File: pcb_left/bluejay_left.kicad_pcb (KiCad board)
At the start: 2 copper layers, 148.3 x 140.5 mm, 81 parts, among them J1 SJ-43514, U1 ATmega328P-PU, Y1 16MHz

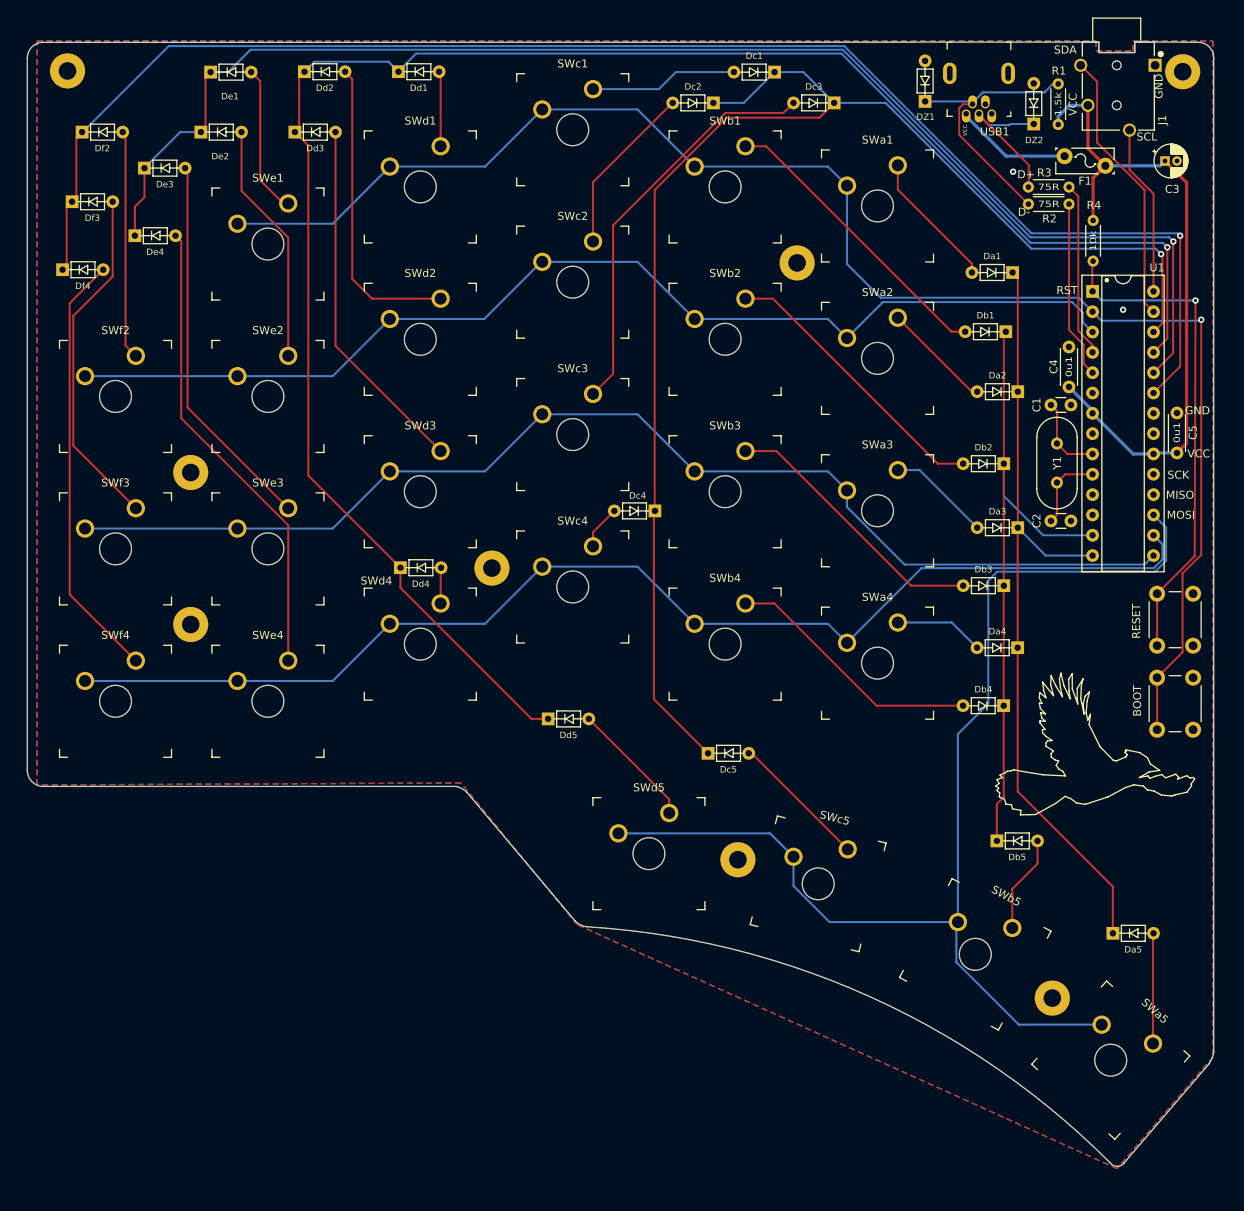
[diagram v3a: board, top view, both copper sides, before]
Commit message: fine tune edge cuts
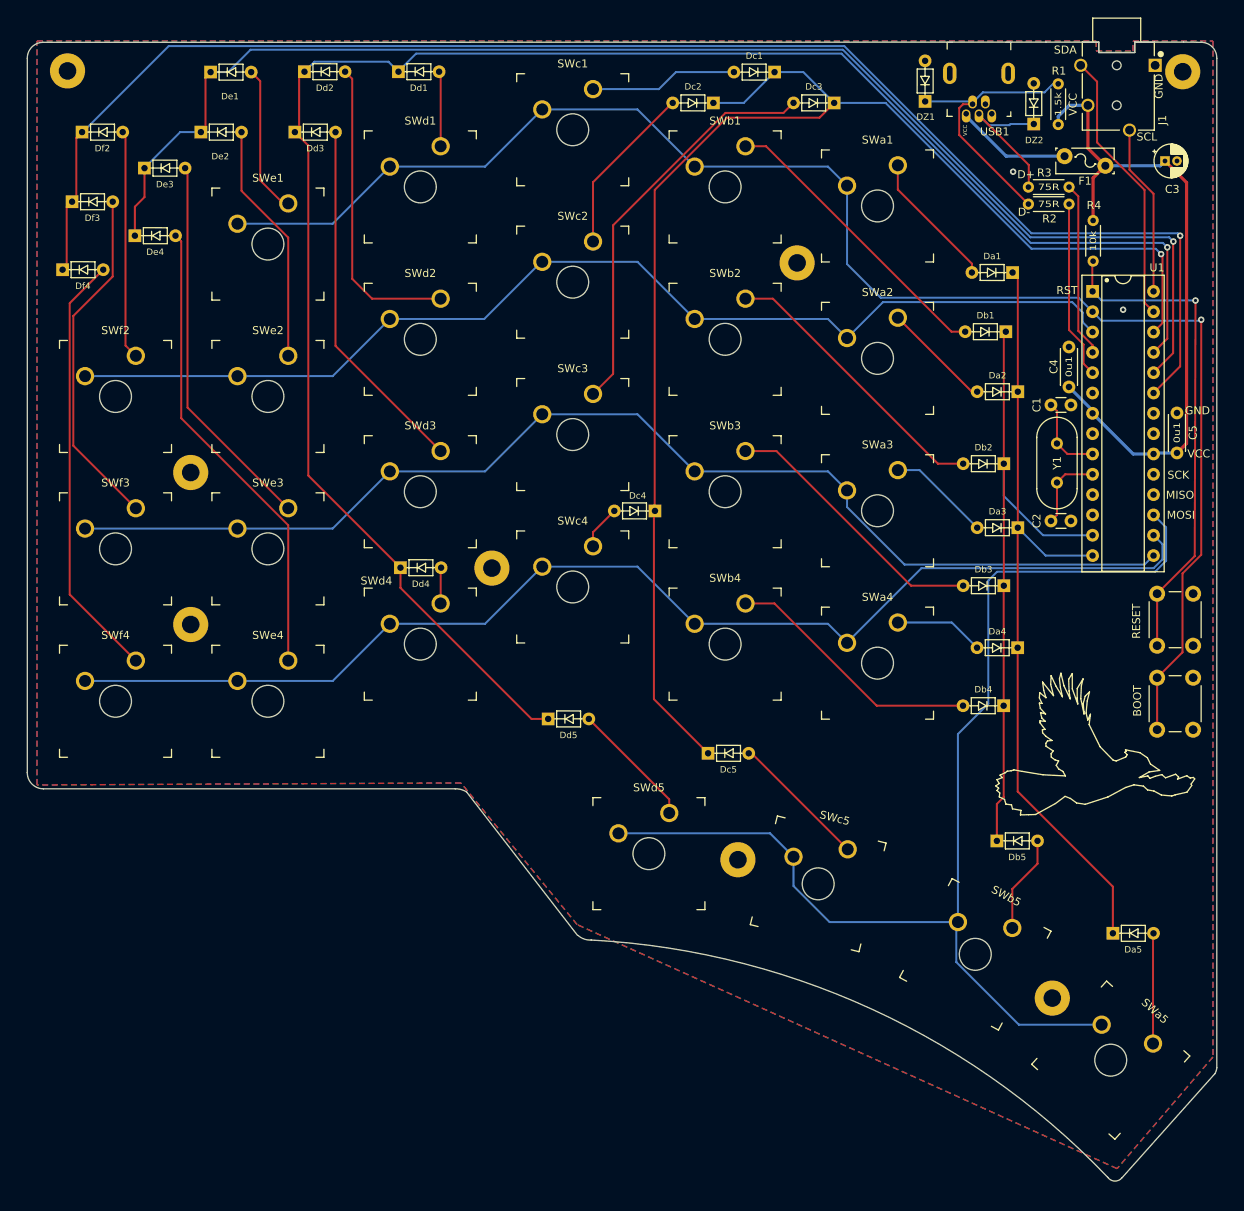
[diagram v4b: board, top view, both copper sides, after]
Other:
- board size 148.3 x 140.5 mm -> 148.7 x 142.4 mm
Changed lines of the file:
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@@
   (gr_line locked (start 26.028999 -42.674998) (end 26.028999 -42.674998) (layer "Eco1.User") (width 0.188976))
   (gr_line locked (start -16.546013 52.286989) (end -16.546013 38.286989) (layer "Eco1.User") (width 0.188976))
-  (gr_line (start 60.48 71.53) (end 49.88 83.9) (layer "Edge.Cuts") (width 0.1))
-  (gr_arc (start -17.32 54.38) (mid 18.101214 63.120674) (end 48.11 83.87) (layer "Edge.Cuts") (width 0.1))
-  (gr_arc (start 59.2 -56.175) (mid 60.553201 -55.55994) (end 61.08 -54.17) (layer "Edge.Cuts") (width 0.1))
-  (gr_line (start 61.08 70.05) (end 61.08 -54.17) (layer "Edge.Cuts") (width 0.1))
+  (gr_line (start 61.23 72.74) (end 49.62 85.75) (layer "Edge.Cuts") (width 0.1))
+  (gr_arc (start -16.74 56.04) (mid 18.380681 64.696706) (end 47.83 85.7) (layer "Edge.Cuts") (width 0.1))
+  (gr_arc (start 59.58 -56.175) (mid 60.933201 -55.55994) (end 61.46 -54.17) (layer "Edge.Cuts") (width 0.1))
+  (gr_line (start 61.46 72) (end 61.46 -54.17) (layer "Edge.Cuts") (width 0.1))
   (gr_arc (start -87.23 -54.18) (mid -86.647749 -55.594848) (end -85.23 -56.17) (layer "Edge.Cuts") (width 0.1))
-  (gr_arc (start -85.23 36.84) (mid -86.648353 36.23717) (end -87.23 34.81) (layer "Edge.Cuts") (width 0.1))
-  (gr_line (start -87.23 -54.18) (end -87.23 34.81) (layer "Edge.Cuts") (width 0.1))
-  (gr_line (start -85.23 36.84) (end -33.72 36.84) (layer "Edge.Cuts") (width 0.1))
-  (gr_line (start -32.31 37.54) (end -18.73 53.68) (layer "Edge.Cuts") (width 0.1))
-  (gr_line (start 59.2 -56.175) (end 57.3 -56.2) (layer "Edge.Cuts") (width 0.1))
-  (gr_arc (start -17.32 54.38) (mid -18.079496 54.13977) (end -18.73 53.68) (layer "Edge.Cuts") (width 0.1))
-  (gr_arc (start 61.08 70.05) (mid 60.863331 70.823783) (end 60.48 71.53) (layer "Edge.Cuts") (width 0.1))
+  (gr_arc (start -85.23 37.14) (mid -86.648353 36.53717) (end -87.23 35.11) (layer "Edge.Cuts") (width 0.1))
+  (gr_line (start -87.23 -54.18) (end -87.23 35.11) (layer "Edge.Cuts") (width 0.1))
+  (gr_line (start -85.23 37.14) (end -33.72 37.14) (layer "Edge.Cuts") (width 0.1))
+  (gr_line (start -32.31 37.54) (end -18.47 55.43) (layer "Edge.Cuts") (width 0.1))
+  (gr_line (start 59.58 -56.175) (end 57.3 -56.2) (layer "Edge.Cuts") (width 0.1))
+  (gr_arc (start -16.74 56.04) (mid -17.619625 55.918116) (end -18.380504 55.46023) (layer "Edge.Cuts") (width 0.1))
+  (gr_arc (start 61.46 72) (mid 61.386012 72.382747) (end 61.23 72.74) (layer "Edge.Cuts") (width 0.1))
   (gr_line (start 40.1 -56.2) (end -85.23 -56.17) (layer "Edge.Cuts") (width 0.1))
-  (gr_arc (start 49.88 83.9) (mid 48.987603 84.321434) (end 48.11 83.87) (layer "Edge.Cuts") (width 0.1))
-  (gr_arc (start -33.72 36.84) (mid -32.960504 37.08023) (end -32.31 37.54) (layer "Edge.Cuts") (width 0.1))
+  (gr_arc (start 49.585572 85.777188) (mid 48.69 86.17) (end 47.833171 85.698624) (layer "Edge.Cuts") (width 0.1))
+  (gr_arc (start -33.72 37.14) (mid -32.98386 37.23023) (end -32.31 37.54) (layer "Edge.Cuts") (width 0.1))
   (gr_text "JLCJLCJLCJLC" (at -80.15 35.09) (layer "B.SilkS")
     (effects (font (size 1 1) (thickness 0.15)) (justify mirror))

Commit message: Update placement of some components and size of drill holes
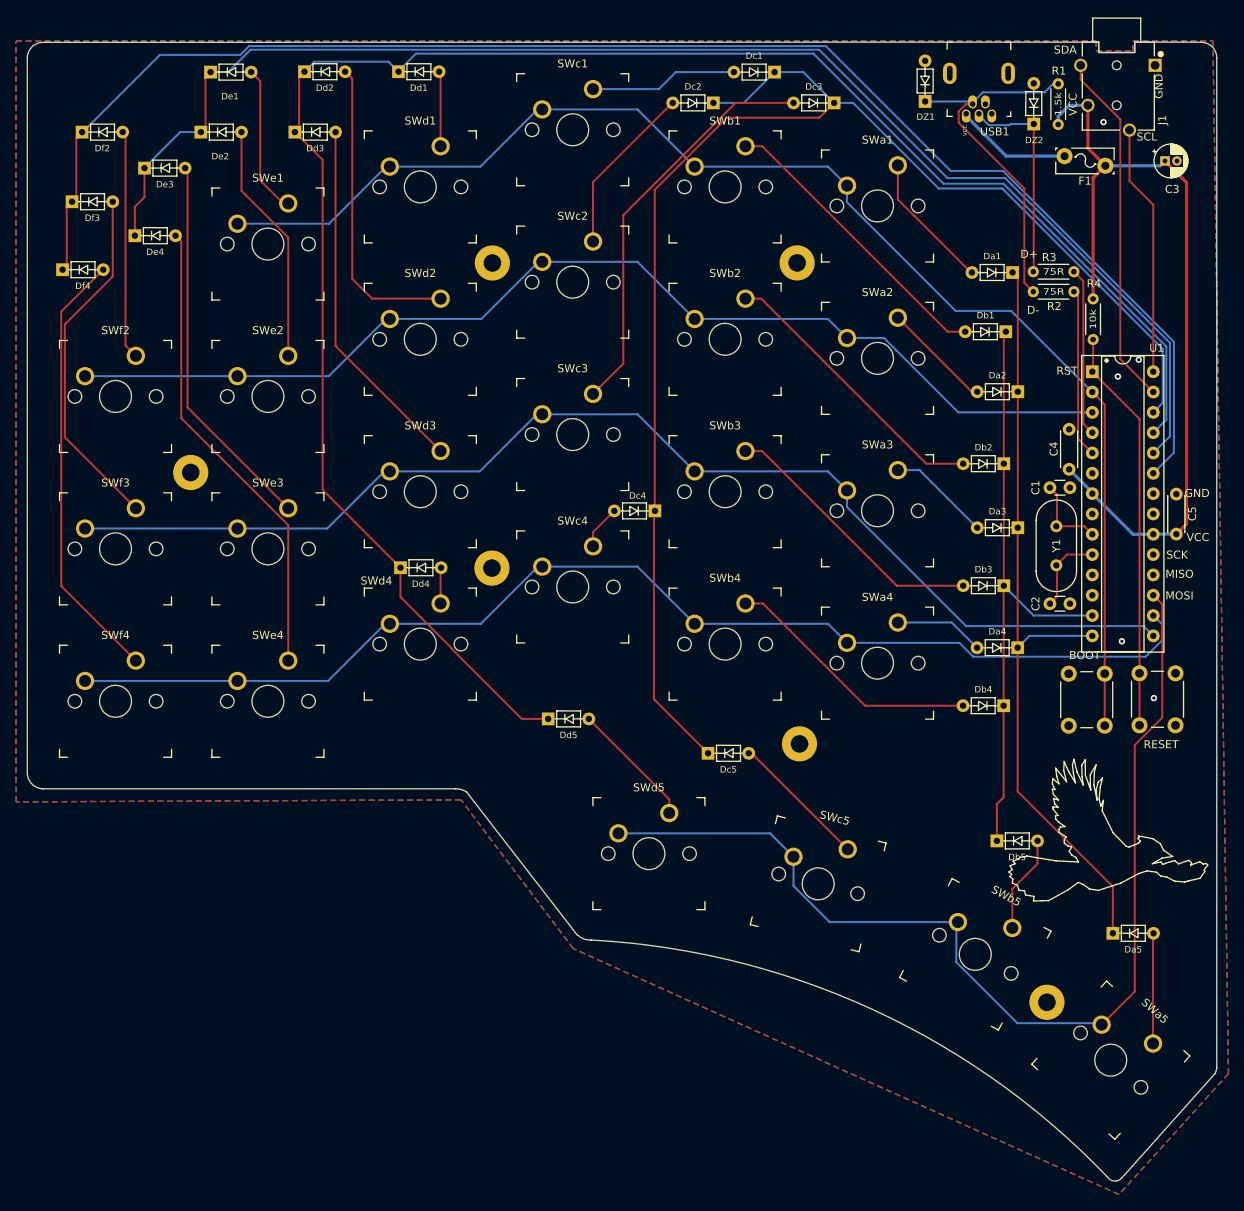
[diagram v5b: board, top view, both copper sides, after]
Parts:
- removed H7, H8: M2, MountingHole:MountingHole_2.2mm_M2_Pad
- C4, C5: value 0u1 -> 100n
- SWa1, SWa2, SWa3, SWa4, SWa5, SWb1, SWb2, SWb3, SWb4, SWb5, SWc1, SWc2, SWc3, SWc4, SWc5, SWd1, SWd2, SWd3, SWd4, SWd5, SWe1, SWe2, SWe3, SWe4, SWf2, SWf3, SWf4: footprint BlueJay footprints:SW_MX_Plate -> BlueJay footprints:SW_MX
- moved H2 117.6 mm to (40.2, 63.8)
- moved H6 77.5 mm to (9.30, 31.5)
- moved H1 58.3 mm to (-29.1, -28.6)
- moved R2 11.0 mm to (43.6, -25.0)
- moved G*** 10.9 mm to (48.4, 45.9)
- moved R3 10.6 mm to (43.6, -27.5)
- moved C1 10.3 mm to (40.6, -0.50)
- moved C2 10.3 mm to (40.6, 14.0)
- moved Y1 10.3 mm to (41.4, 9.20)
- moved C4 10.3 mm to (43.0, -2.80)
- moved PB1 10.2 mm to (51.8, 29.2)
- moved C5 10.1 mm to (56.4, 5.30)
- moved U1 10.0 mm to (45.9, -15.0)
- moved R4 9.80 mm to (46.0, -24.1)
- moved PB2 9.59 mm to (47.5, 22.8), turned to -90 degrees
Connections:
- H2 pad 1: GND -> (no net)
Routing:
- net /row1: track 196.7 -> 171.0 mm, vias 1 -> 0
- net VCC: track 84.2 -> 103.8 mm
- net /row5: track 149.6 -> 132.9 mm
- net Net-(PB1-Pad1): track 62.3 -> 50.7 mm, vias 1 -> 0
- net /USBPRE_D-: track 35.4 -> 46.5 mm
- net /i2c_SCL: track 21.4 -> 31.4 mm
- net /i2c_SDA: track 34.6 -> 44.6 mm
- net /USBPRE_D+: track 19.4 -> 26.1 mm
- net /colB: track 81.3 -> 76.7 mm
- net /colD: track 229.5 -> 232.8 mm, vias 1 -> 0
- net /colC: track 177.5 -> 180.8 mm, vias 1 -> 0
- net /row3: track 148.9 -> 152.1 mm
- net /row4: track 152.4 -> 149.6 mm
- net /colE: track 174.8 -> 176.8 mm, vias 1 -> 0
- net /USB_D-: track 22.3 -> 21.1 mm
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
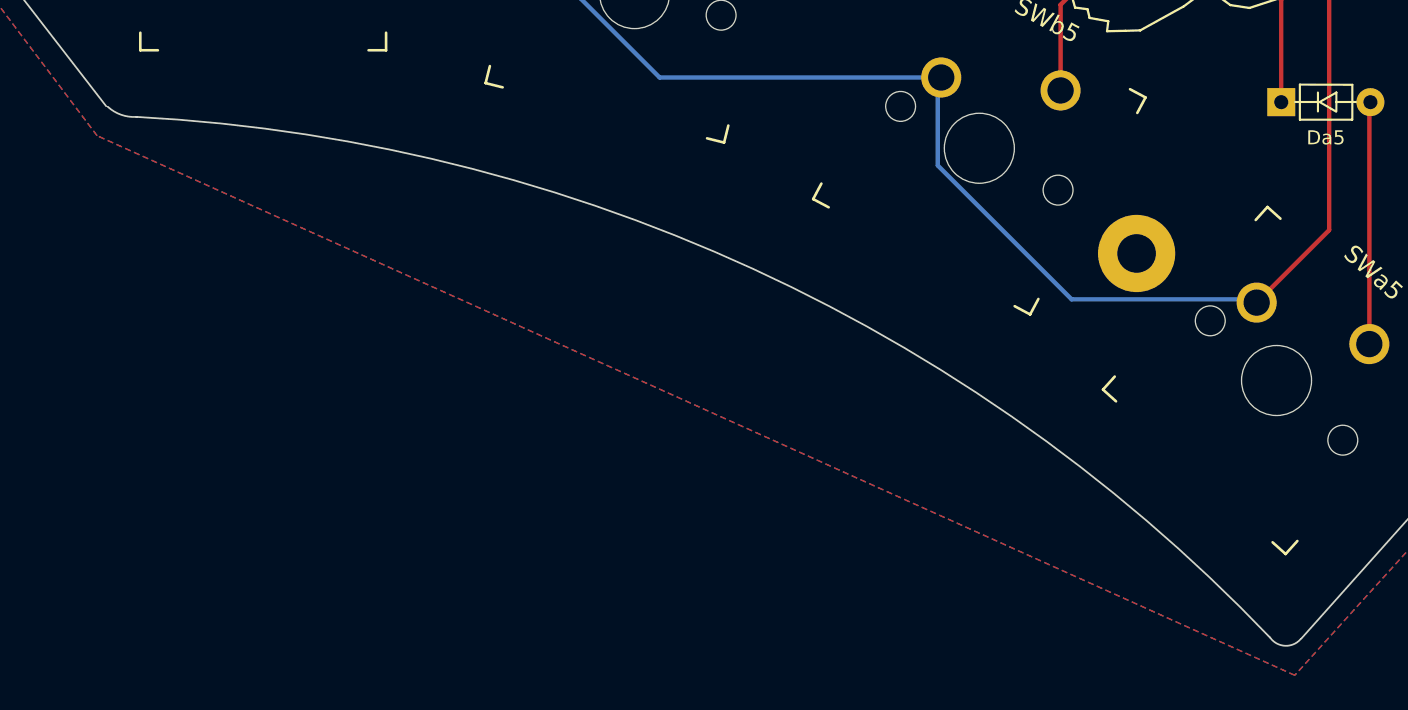
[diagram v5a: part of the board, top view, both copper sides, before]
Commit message: Fine tune edge cut
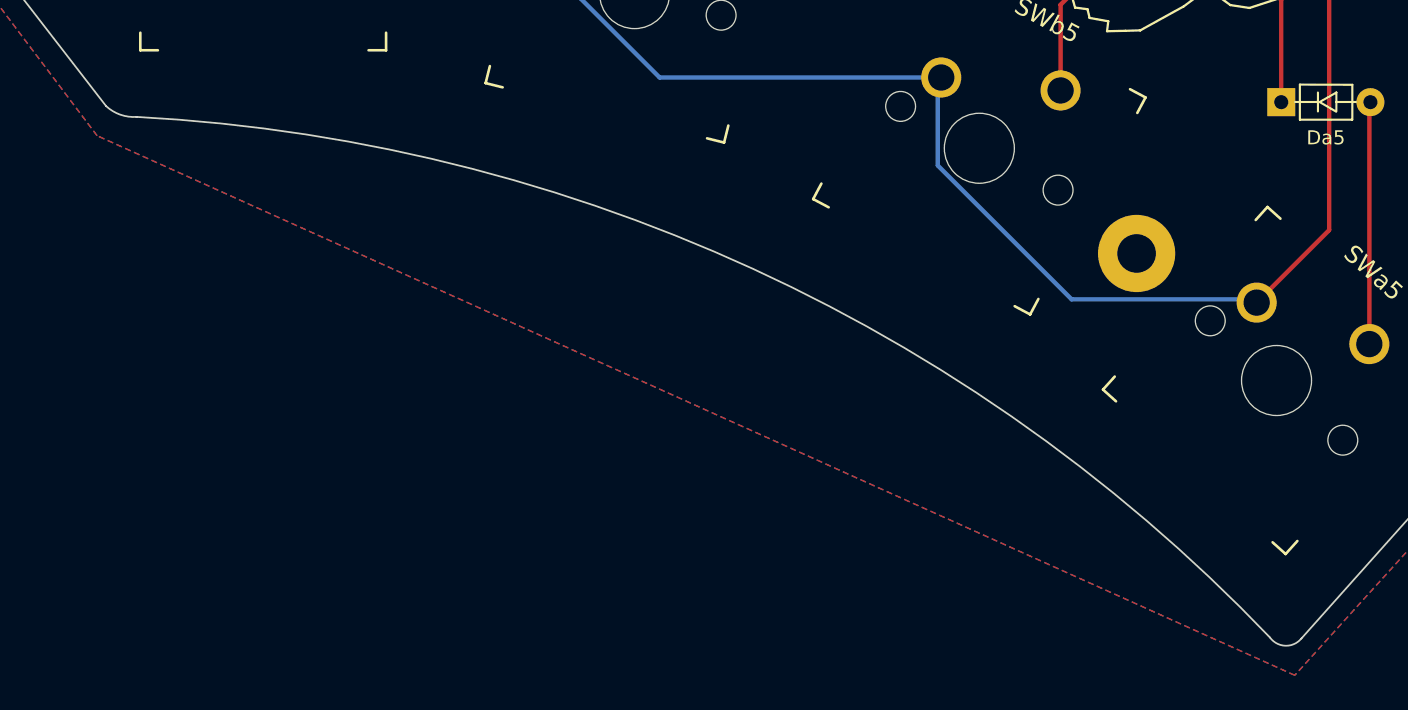
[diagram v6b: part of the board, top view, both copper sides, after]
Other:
- outline, holes or cut-outs redrawn
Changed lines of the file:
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@@
   (gr_line (start -32.31 37.54) (end -18.47 55.43) (layer "Edge.Cuts") (width 0.1))
   (gr_line (start 59.58 -56.175) (end 57.3 -56.2) (layer "Edge.Cuts") (width 0.1))
-  (gr_arc (start -16.74 56.04) (mid -17.619625 55.918116) (end -18.380504 55.46023) (layer "Edge.Cuts") (width 0.1))
+  (gr_arc (start -16.74 56.04) (mid -17.667469 55.912166) (end -18.47 55.43) (layer "Edge.Cuts") (width 0.1))
   (gr_arc (start 61.46 72) (mid 61.386012 72.382747) (end 61.23 72.74) (layer "Edge.Cuts") (width 0.1))
   (gr_line (start 40.1 -56.2) (end -85.23 -56.17) (layer "Edge.Cuts") (width 0.1))
-  (gr_arc (start 49.585572 85.777188) (mid 48.69 86.17) (end 47.833171 85.698624) (layer "Edge.Cuts") (width 0.1))
+  (gr_arc (start 49.62 85.75) (mid 48.712671 86.166365) (end 47.83 85.7) (layer "Edge.Cuts") (width 0.1))
   (gr_arc (start -33.72 37.14) (mid -32.98386 37.23023) (end -32.31 37.54) (layer "Edge.Cuts") (width 0.1))
   (gr_text "JLCJLCJLCJLC" (at -80.15 35.09) (layer "B.SilkS")

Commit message: Update gerber files
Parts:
- removed G***: LOGO, BlueJay footprints:BlueJay_Logo_New_Small
- added Ref**: Val**, BlueJay footprints:BlueJay in Halfomania font, F.Cu at (43.7, 37.9)
